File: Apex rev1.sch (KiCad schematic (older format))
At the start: 22 parts, among them J1 OLED, SW1 SW_PUSH, SW2 Rotary_Encoder_Switch, U1 AT90USB1286-MU, Y1 8MHz

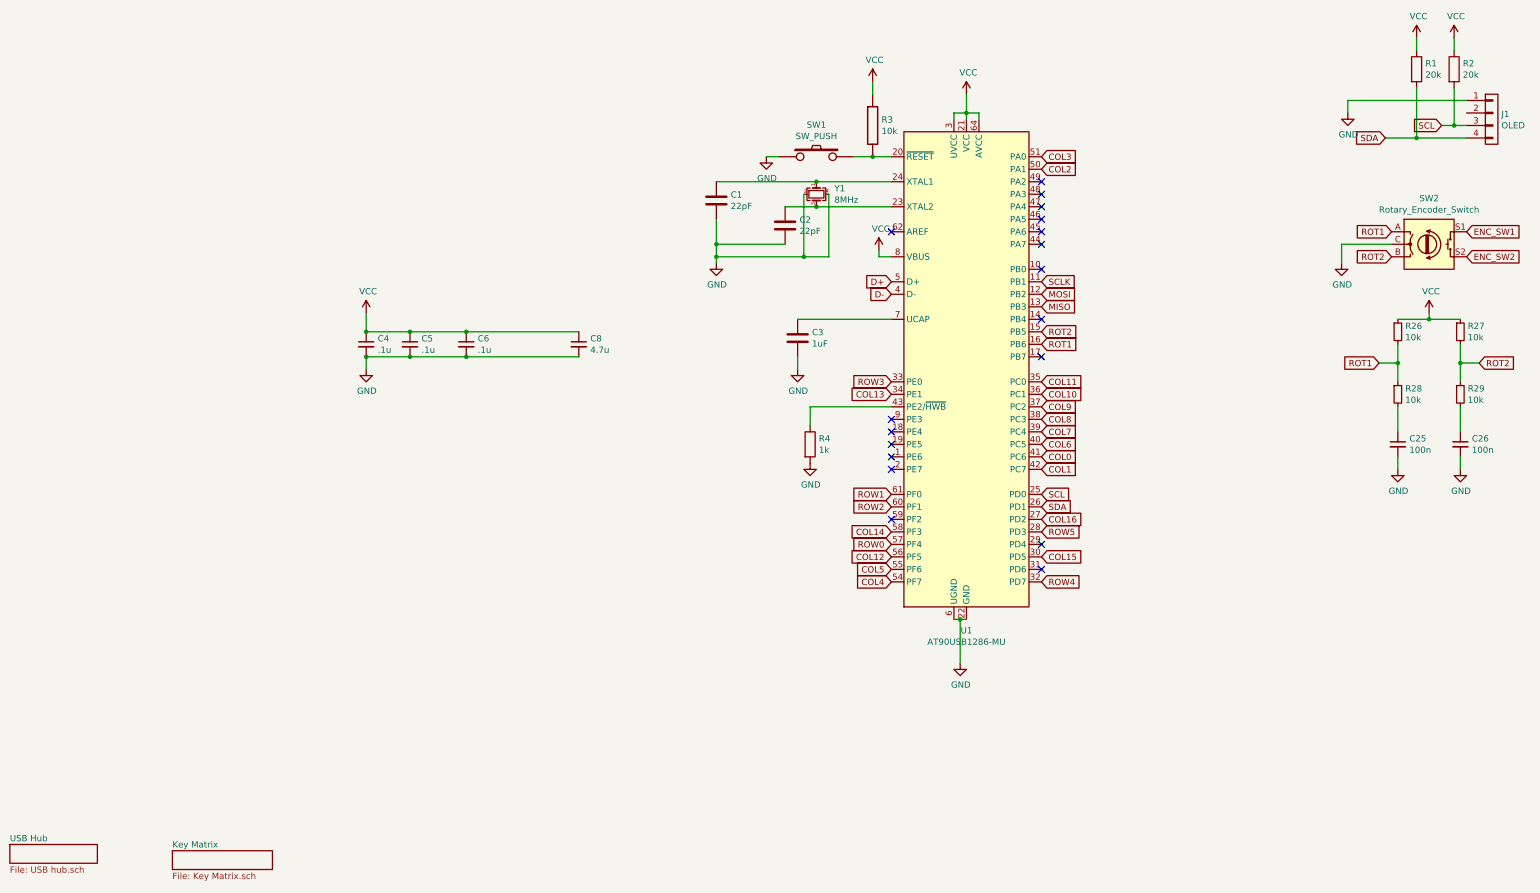
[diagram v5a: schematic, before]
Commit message: Add ISP header
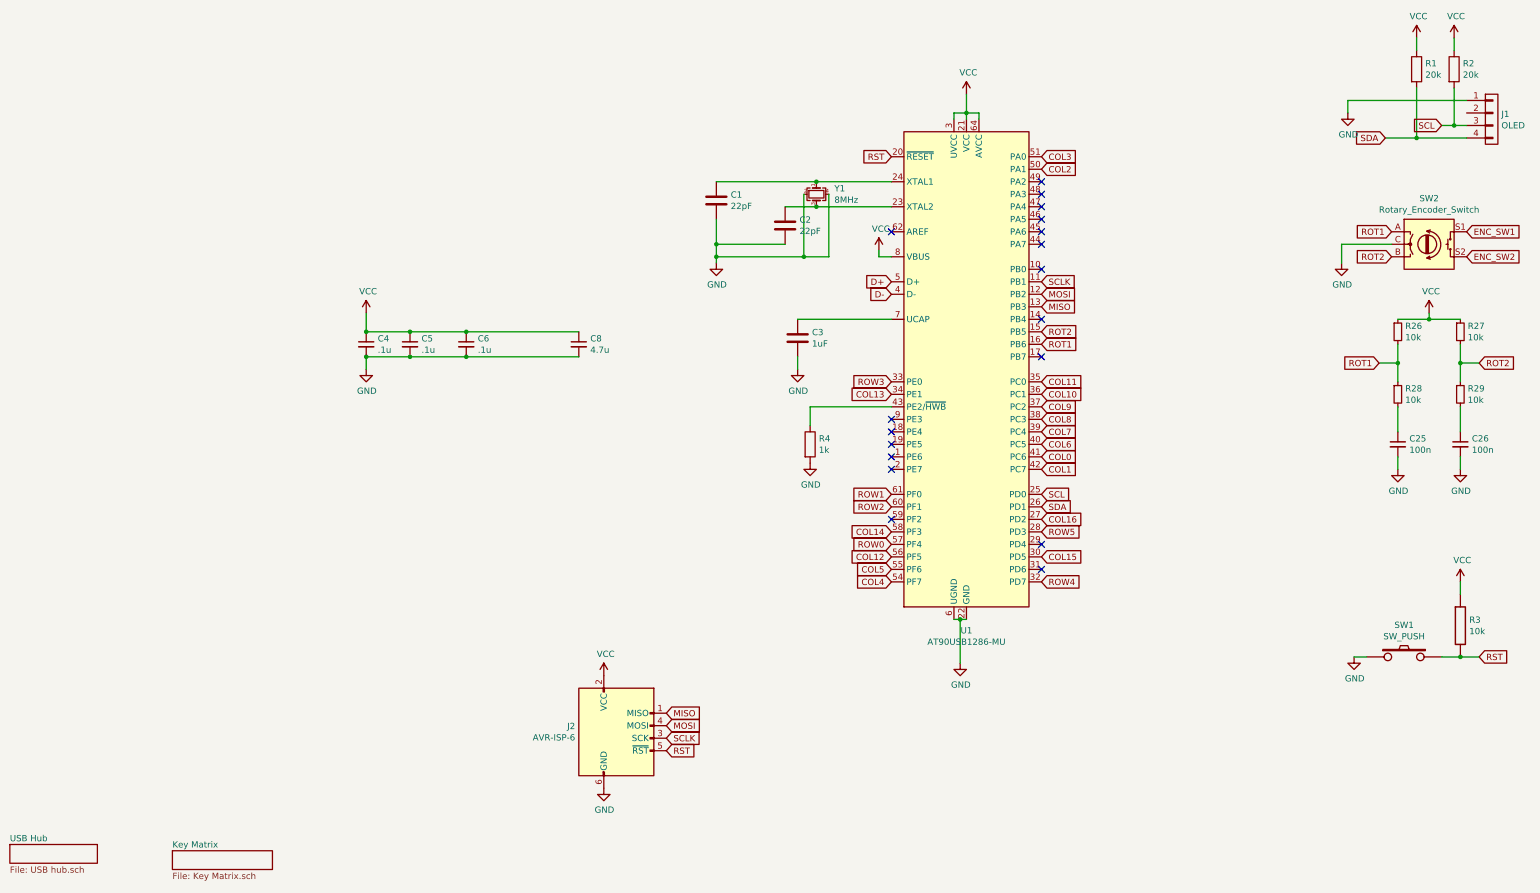
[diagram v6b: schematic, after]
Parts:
- added J2: AVR-ISP-6, 1_Keyboard Footprints:ICSP-Header, symbol Connector:AVR-ISP-6
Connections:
- net GND: now also J2.6 (GND)
- net MISO: now also J2.1 (MISO)
- net MOSI: now also J2.4 (MOSI)
- net SCLK: now also J2.3 (SCK)
- net VCC: now also J2.2 (VCC)
- net RST: now reaches R3.2, SW1.2, U1.20 (~RESET)
- net RST: now also J2.5 (~RST)
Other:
- moved on the sheet: R3, SW1
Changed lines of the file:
@@
 $EndComp
 Wire Wire Line
-	8400 1750 8250 1750
+	13100 5750 12950 5750
 $Comp
 L Apex-rev1-rescue:R-keyboard_parts R3
 U 1 1 5EFE3710
-P 8250 1500
-F 0 "R3" H 8321 1546 50  0000 L CNN
-F 1 "10k" H 8321 1455 50  0000 L CNN
-F 2 "1_Keyboard Footprints:R_0603" H 8250 1500 60  0001 C CNN
-F 3 "" H 8250 1500 60  0000 C CNN
-	1    8250 1500
-	1    0    0    -1
-$EndComp
-Wire Wire Line
-	8250 1750 8100 1750
-Connection ~ 8250 1750
+P 12950 5500
+F 0 "R3" H 13021 5546 50  0000 L CNN
+F 1 "10k" H 13021 5455 50  0000 L CNN
+F 2 "1_Keyboard Footprints:R_0603" H 12950 5500 60  0001 C CNN
+F 3 "" H 12950 5500 60  0000 C CNN
+	1    12950 5500
+	1    0    0    -1
+$EndComp
+Wire Wire Line
+	12950 5750 12800 5750
+Connection ~ 12950 5750
 $Comp
 L Apex-rev1-rescue:SW_PUSH-keyboard_parts SW1
 U 1 1 5EFE4C93
-P 7800 1750
-F 0 "SW1" H 7800 2005 50  0000 C CNN
-F 1 "SW_PUSH" H 7800 1914 50  0000 C CNN
-F 2 "1_Keyboard Footprints:SKQG-1155865" H 7800 1750 60  0001 C CNN
-F 3 "" H 7800 1750 60  0000 C CNN
-	1    7800 1750
+P 12500 5750
+F 0 "SW1" H 12500 6005 50  0000 C CNN
+F 1 "SW_PUSH" H 12500 5914 50  0000 C CNN
+F 2 "1_Keyboard Footprints:SKQG-1155865" H 12500 5750 60  0001 C CNN
+F 3 "" H 12500 5750 60  0000 C CNN
+	1    12500 5750
 	1    0    0    -1
 $EndComp
@@
 L power:GND #PWR0102
 U 1 1 5EFE56D1
-P 7400 1750
-F 0 "#PWR0102" H 7400 1500 50  0001 C CNN
-F 1 "GND" H 7405 1577 50  0000 C CNN
-F 2 "" H 7400 1750 50  0001 C CNN
-F 3 "" H 7400 1750 50  0001 C CNN
-	1    7400 1750
-	1    0    0    -1
-$EndComp
-Wire Wire Line
-	8250 1250 8250 1150
+P 12100 5750
+F 0 "#PWR0102" H 12100 5500 50  0001 C CNN
+F 1 "GND" H 12105 5577 50  0000 C CNN
+F 2 "" H 12100 5750 50  0001 C CNN
+F 3 "" H 12100 5750 50  0001 C CNN
+	1    12100 5750
+	1    0    0    -1
+$EndComp
+Wire Wire Line
+	12950 5250 12950 5150
 $Comp
 L power:VCC #PWR0103
 U 1 1 5EFE6069
-P 8250 1150
-F 0 "#PWR0103" H 8250 1000 50  0001 C CNN
-F 1 "VCC" H 8265 1323 50  0000 C CNN
-F 2 "" H 8250 1150 50  0001 C CNN
-F 3 "" H 8250 1150 50  0001 C CNN
-	1    8250 1150
+P 12950 5150
+F 0 "#PWR0103" H 12950 5000 50  0001 C CNN
+F 1 "VCC" H 12965 5323 50  0000 C CNN
+F 2 "" H 12950 5150 50  0001 C CNN
+F 3 "" H 12950 5150 50  0001 C CNN
+	1    12950 5150
 	1    0    0    -1
 $EndComp
@@
 	9000 1250 9000 1400
 Wire Wire Line
-	7400 1750 7500 1750
+	12100 5750 12200 5750
 $Comp
 L Device:C C1
@@
 Text GLabel 9600 1850 2    50   Input ~ 0
 COL2
+$Comp
+L Connector:AVR-ISP-6 J2
+U 1 1 5F164554
+P 6200 6400
+F 0 "J2" H 5871 6496 50  0000 R CNN
+F 1 "AVR-ISP-6" H 5871 6405 50  0000 R CNN
+F 2 "1_Keyboard Footprints:ICSP-Header" V 5950 6450 50  0001 C CNN
+F 3 " ~" H 4925 5850 50  0001 C CNN
+	1    6200 6400
+	1    0    0    -1
+$EndComp
+Text GLabel 6600 6300 2    50   Input ~ 0
+MOSI
+Text GLabel 6600 6200 2    50   Input ~ 0
+MISO
+Text GLabel 6600 6400 2    50   Input ~ 0
+SCLK
+Text GLabel 13100 5750 2    50   Input ~ 0
+RST
+Text GLabel 8400 1750 0    50   Input ~ 0
+RST
+Text GLabel 6600 6500 2    50   Input ~ 0
+RST
+$Comp
+L power:GND #PWR0116
+U 1 1 5F16E6E7
+P 6100 6800
+F 0 "#PWR0116" H 6100 6550 50  0001 C CNN
+F 1 "GND" H 6105 6627 50  0000 C CNN
+F 2 "" H 6100 6800 50  0001 C CNN
+F 3 "" H 6100 6800 50  0001 C CNN
+	1    6100 6800
+	1    0    0    -1
+$EndComp
+$Comp
+L power:VCC #PWR0130
+U 1 1 5F16F036
+P 6100 5900
+F 0 "#PWR0130" H 6100 5750 50  0001 C CNN
+F 1 "VCC" H 6115 6073 50  0000 C CNN
+F 2 "" H 6100 5900 50  0001 C CNN
+F 3 "" H 6100 5900 50  0001 C CNN
+	1    6100 5900
+	1    0    0    -1
+$EndComp
 $EndSCHEMATC

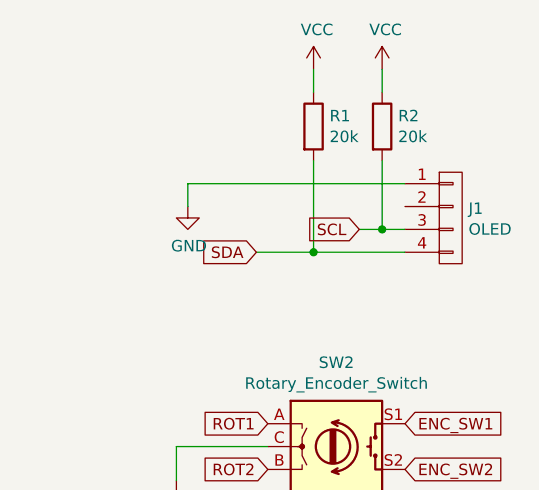
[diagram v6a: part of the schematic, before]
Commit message: refined silkscreens
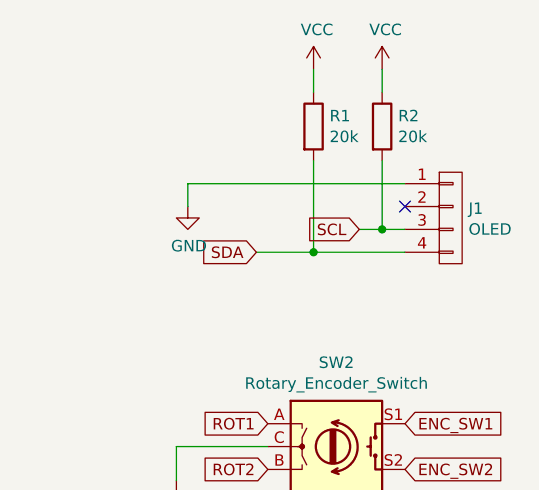
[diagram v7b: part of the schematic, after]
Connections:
- no-connect marks 18 -> 19
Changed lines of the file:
@@
 	1    0    0    -1
 $EndComp
+NoConn ~ 13000 1400
 $EndSCHEMATC
